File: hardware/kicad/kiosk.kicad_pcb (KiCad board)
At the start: 2 copper layers, 158 x 121 mm, 20 parts, among them J10 TerminalBlock_MaiXu_MX126-5.0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, J11 TerminalBlock_MaiXu_MX126-5.0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, J13 PinHeader_1x09_P2.54mm_Vertic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, J14 PinHeader_1x04_P2.54mm_Vertic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, J3 PinSocket_1x14_P2.54mm_Vertic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, J4 PinSocket_1x06_P2.54mm_Vertic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, J5 PinSocket_1x04_P2.54mm_Vertic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, J6 PinSocket_1x06_P2.54mm_Vertic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, J7 PinSocket_1x07_P2.54mm_Vertic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, J9 PinHeader_1x03_P2.54mm_Vertic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, U1 ESP32-S3-CAM

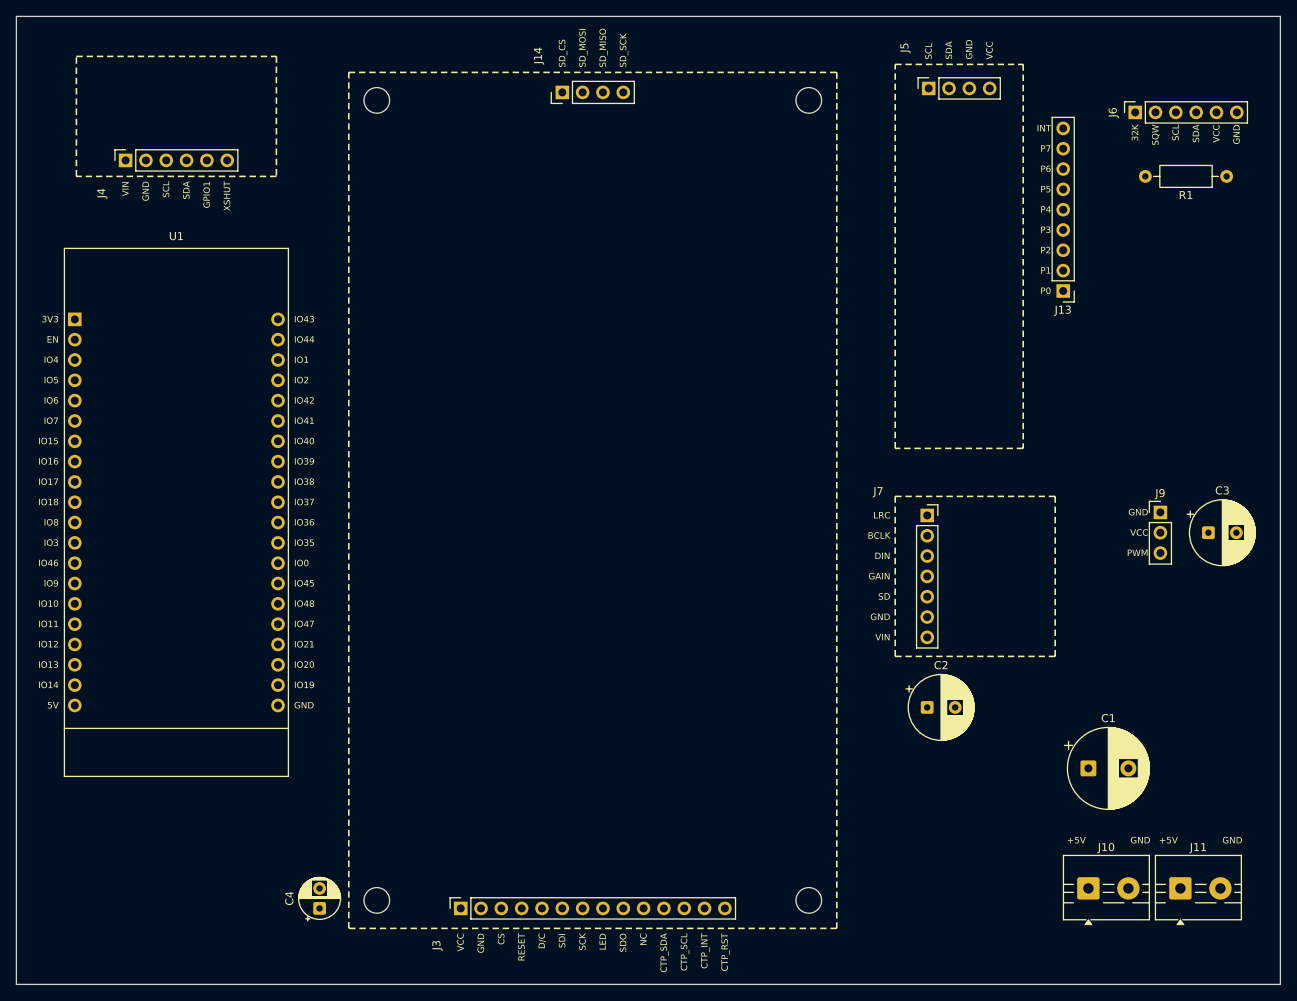
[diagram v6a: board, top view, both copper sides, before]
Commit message: fix(hardware): start every top-row module body on the panel's top edge
The VL53L1X outline began 2 mm above the panel's and the expander's 1 mm
above it. Neither offset was a decision — they are the numbers that were
typed during the rough placement and never revisited — and three
rectangles starting within 2 mm of each other reads as a board nobody
lined up, which is what it was.

All three now start at y 7. The devkit follows the ToF down so the left
column keeps its spacing, and the gap between the ToF's body and the
devkit's courtyard stays 8.75 mm.

Task: E14-T8
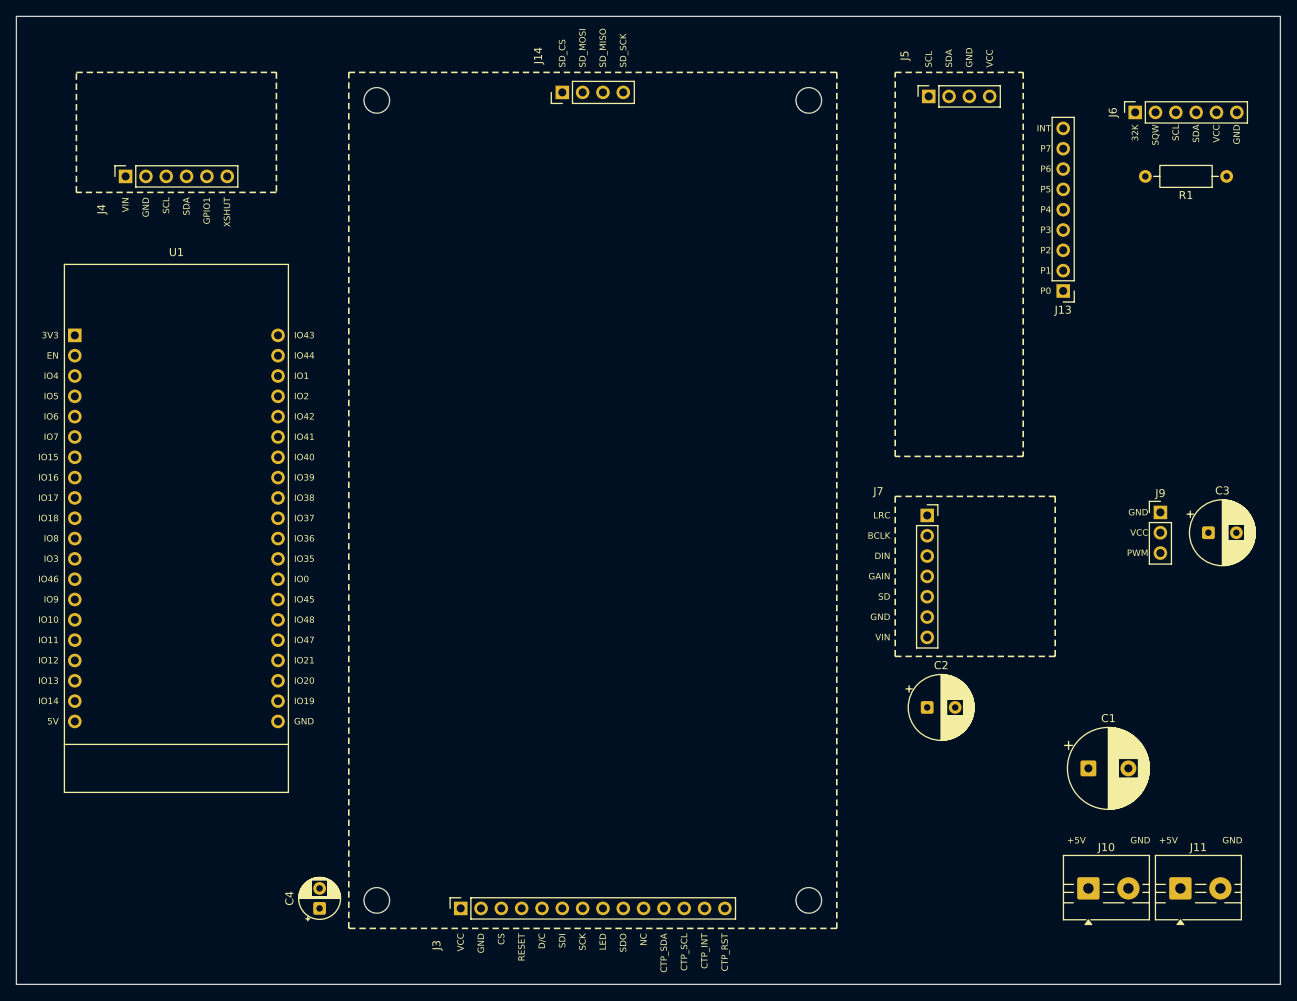
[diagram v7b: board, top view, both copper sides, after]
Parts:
- moved J4 2.00 mm to (13.7, 20.0)
- moved U1 2.00 mm to (20.0, 64.0)
- moved J5 1.00 mm to (114.0, 10.0)
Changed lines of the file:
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@@
 	(footprint "Connector_PinSocket_2.54mm:PinSocket_1x04_P2.54mm_Vertical"
 		(layer "F.Cu")
-		(at 114.04 9 90)
+		(at 114.04 10 90)
 		(descr "Through hole straight socket strip, 1x04, 2.54mm pitch, single row (from Kicad 4.0.7), script generated")
 		(tags "Through hole socket strip THT 1x04 2.54mm single row")
@@
 	(footprint "Connector_PinSocket_2.54mm:PinSocket_1x06_P2.54mm_Vertical"
 		(layer "F.Cu")
-		(at 13.65 18 90)
+		(at 13.65 20 90)
 		(descr "Through hole straight socket strip, 1x06, 2.54mm pitch, single row (from Kicad 4.0.7), script generated")
 		(tags "Through hole socket strip THT 1x06 2.54mm single row")
@@
 	(footprint "kiosk:ESP32-S3-CAM_2x20_P2.54mm_R25.4mm"
 		(layer "F.Cu")
-		(at 20 62)
+		(at 20 64)
 		(descr "GOOUUU ESP32-S3-CAM socket, 2x20 at 2.54 mm, rows 25.4 mm apart - measured on the board and confirmed against a published figure. Pin 1 = 3V3 at top left seen from above with the two USB-C on the bottom edge; the silkscreen bar marks that edge. The outline is deliberately oversized: this board has no datasheet, so its real edge is unmeasured and the courtyard errs wide to keep tall parts out from under it. Keep the USB edge clear for cables, and EN and BOOT reachable on the top face.")
 		(tags "esp32s3 cam devkit socket")
@@
 	)
 	(gr_line
-		(start 7.5 5)
-		(end 32.5 5)
+		(start 7.5 7)
+		(end 32.5 7)
 		(stroke
 			(width 0.2)
@@
 	)
 	(gr_line
-		(start 7.5 20)
-		(end 7.5 5)
+		(start 7.5 22)
+		(end 7.5 7)
 		(stroke
 			(width 0.2)
@@
 	)
 	(gr_line
-		(start 32.5 5)
-		(end 32.5 20)
+		(start 32.5 7)
+		(end 32.5 22)
 		(stroke
 			(width 0.2)
@@
 	)
 	(gr_line
-		(start 32.5 20)
-		(end 7.5 20)
+		(start 32.5 22)
+		(end 7.5 22)
 		(stroke
 			(width 0.2)
@@
 	)
 	(gr_line
-		(start 109.85 6)
-		(end 125.85 6)
+		(start 109.85 7)
+		(end 125.85 7)
 		(stroke
 			(width 0.2)
@@
 	)
 	(gr_line
-		(start 109.85 54)
-		(end 109.85 6)
+		(start 109.85 55)
+		(end 109.85 7)
 		(stroke
 			(width 0.2)
@@
 	)
 	(gr_line
-		(start 125.85 6)
-		(end 125.85 54)
+		(start 125.85 7)
+		(end 125.85 55)
 		(stroke
 			(width 0.2)
@@
 	)
 	(gr_line
-		(start 125.85 54)
-		(end 109.85 54)
+		(start 125.85 55)
+		(end 109.85 55)
 		(stroke
 			(width 0.2)
@@
 	)
 	(gr_text "IO43"
-		(at 34.7 37.87 0)
+		(at 34.7 39.87 0)
 		(layer "F.SilkS")
 		(effects
@@
 	)
 	(gr_text "IO44"
-		(at 34.7 40.41 0)
+		(at 34.7 42.41 0)
 		(layer "F.SilkS")
 		(effects
@@
 	)
 	(gr_text "IO1"
-		(at 34.7 42.95 0)
+		(at 34.7 44.95 0)
 		(layer "F.SilkS")
 		(effects
@@
 	)
 	(gr_text "IO2"
-		(at 34.7 45.49 0)
+		(at 34.7 47.49 0)
 		(layer "F.SilkS")
 		(effects
@@
 	)
 	(gr_text "IO42"
-		(at 34.7 48.03 0)
+		(at 34.7 50.03 0)
 		(layer "F.SilkS")
 		(effects
@@
 	)
 	(gr_text "IO41"
-		(at 34.7 50.57 0)
+		(at 34.7 52.57 0)
 		(layer "F.SilkS")
 		(effects
@@
 	)
 	(gr_text "IO40"
-		(at 34.7 53.11 0)
+		(at 34.7 55.11 0)
 		(layer "F.SilkS")
 		(effects
@@
 	)
 	(gr_text "IO39"
-		(at 34.7 55.65 0)
+		(at 34.7 57.65 0)
 		(layer "F.SilkS")
 		(effects
@@
 	)
 	(gr_text "IO38"
-		(at 34.7 58.19 0)
+		(at 34.7 60.19 0)
 		(layer "F.SilkS")
 		(effects
@@
 	)
 	(gr_text "IO37"
-		(at 34.7 60.73 0)
+		(at 34.7 62.73 0)
 		(layer "F.SilkS")
 		(effects
@@
 	)
 	(gr_text "IO36"
-		(at 34.7 63.27 0)
+		(at 34.7 65.27 0)
 		(layer "F.SilkS")
 		(effects
@@
 	)
 	(gr_text "IO35"
-		(at 34.7 65.81 0)
+		(at 34.7 67.81 0)
 		(layer "F.SilkS")
 		(effects
@@
 	)
 	(gr_text "IO0"
-		(at 34.7 68.35 0)
+		(at 34.7 70.35 0)
 		(layer "F.SilkS")
 		(effects
@@
 	)
 	(gr_text "IO45"
-		(at 34.7 70.89 0)
+		(at 34.7 72.89 0)
 		(layer "F.SilkS")
 		(effects
@@
 	)
 	(gr_text "IO48"
-		(at 34.7 73.43 0)
+		(at 34.7 75.43 0)
 		(layer "F.SilkS")
 		(effects
@@
 	)
 	(gr_text "IO47"
-		(at 34.7 75.97 0)
+		(at 34.7 77.97 0)
 		(layer "F.SilkS")
 		(effects
@@
 	)
 	(gr_text "IO21"
-		(at 34.7 78.51 0)
+		(at 34.7 80.51 0)
 		(layer "F.SilkS")
 		(effects
@@
 	)
 	(gr_text "IO20"
-		(at 34.7 81.05 0)
+		(at 34.7 83.05 0)
 		(layer "F.SilkS")
 		(effects
@@
 	)
 	(gr_text "IO19"
-		(at 34.7 83.59 0)
+		(at 34.7 85.59 0)
 		(layer "F.SilkS")
 		(effects
@@
 	)
 	(gr_text "GND"
-		(at 34.7 86.13 0)
+		(at 34.7 88.13 0)
 		(layer "F.SilkS")
 		(effects
@@
 	)
 	(gr_text "3V3"
-		(at 5.3 37.87 0)
+		(at 5.3 39.87 0)
 		(layer "F.SilkS")
 		(effects
@@
 	)
 	(gr_text "EN"
-		(at 5.3 40.41 0)
+		(at 5.3 42.41 0)
 		(layer "F.SilkS")
 		(effects
@@
 	)
 	(gr_text "IO4"
-		(at 5.3 42.95 0)
+		(at 5.3 44.95 0)
 		(layer "F.SilkS")
 		(effects
@@
 	)
 	(gr_text "IO5"
-		(at 5.3 45.49 0)
+		(at 5.3 47.49 0)
 		(layer "F.SilkS")
 		(effects
@@
 	)
 	(gr_text "IO6"
-		(at 5.3 48.03 0)
+		(at 5.3 50.03 0)
 		(layer "F.SilkS")
 		(effects
@@
 	)
 	(gr_text "IO7"
-		(at 5.3 50.57 0)
+		(at 5.3 52.57 0)
 		(layer "F.SilkS")
 		(effects
@@
 	)
 	(gr_text "IO15"
-		(at 5.3 53.11 0)
+		(at 5.3 55.11 0)
 		(layer "F.SilkS")
 		(effects
@@
 	)
 	(gr_text "IO16"
-		(at 5.3 55.65 0)
+		(at 5.3 57.65 0)
 		(layer "F.SilkS")
 		(effects
@@
 	)
 	(gr_text "IO17"
-		(at 5.3 58.19 0)
+		(at 5.3 60.19 0)
 		(layer "F.SilkS")
 		(effects
@@
 	)
 	(gr_text "IO18"
-		(at 5.3 60.73 0)
+		(at 5.3 62.73 0)
 		(layer "F.SilkS")
 		(effects
@@
 	)
 	(gr_text "IO8"
-		(at 5.3 63.27 0)
+		(at 5.3 65.27 0)
 		(layer "F.SilkS")
 		(effects
@@
 	)
 	(gr_text "IO3"
-		(at 5.3 65.81 0)
+		(at 5.3 67.81 0)
 		(layer "F.SilkS")
 		(effects
@@
 	)
 	(gr_text "IO46"
-		(at 5.3 68.35 0)
+		(at 5.3 70.35 0)
 		(layer "F.SilkS")
 		(effects
@@
 	)
 	(gr_text "IO9"
-		(at 5.3 70.89 0)
+		(at 5.3 72.89 0)
 		(layer "F.SilkS")
 		(effects
@@
 	)
 	(gr_text "IO10"
-		(at 5.3 73.43 0)
+		(at 5.3 75.43 0)
 		(layer "F.SilkS")
 		(effects
@@
 	)
 	(gr_text "IO11"
-		(at 5.3 75.97 0)
+		(at 5.3 77.97 0)
 		(layer "F.SilkS")
 		(effects
@@
 	)
 	(gr_text "IO12"
-		(at 5.3 78.51 0)
+		(at 5.3 80.51 0)
 		(layer "F.SilkS")
 		(effects
@@
 	)
 	(gr_text "IO13"
-		(at 5.3 81.05 0)
+		(at 5.3 83.05 0)
 		(layer "F.SilkS")
 		(effects
@@
 	)
 	(gr_text "IO14"
-		(at 5.3 83.59 0)
+		(at 5.3 85.59 0)
 		(layer "F.SilkS")
 		(effects
@@
 	)
 	(gr_text "5V"
-		(at 5.3 86.13 0)
+		(at 5.3 88.13 0)
 		(layer "F.SilkS")
 		(effects
@@
 	)
 	(gr_text "SCL"
-		(at 114.04 5.4 90)
+		(at 114.04 6.4 90)
 		(layer "F.SilkS")
 		(effects
@@
 	)
 	(gr_text "SDA"
-		(at 116.58 5.4 90)
+		(at 116.58 6.4 90)
 		(layer "F.SilkS")
 		(effects
@@
 	)
 	(gr_text "GND"
-		(at 119.12 5.4 90)
+		(at 119.12 6.4 90)
 		(layer "F.SilkS")
 		(effects
@@
 	)
 	(gr_text "VCC"
-		(at 121.66 5.4 90)
+		(at 121.66 6.4 90)
 		(layer "F.SilkS")
 		(effects
@@
 	)
 	(gr_text "VIN"
-		(at 13.65 20.6 90)
+		(at 13.65 22.6 90)
 		(layer "F.SilkS")
 		(effects
@@
 	)
 	(gr_text "GND"
-		(at 16.19 20.6 90)
+		(at 16.19 22.6 90)
 		(layer "F.SilkS")
 		(effects
@@
 	)
 	(gr_text "SCL"
-		(at 18.73 20.6 90)
+		(at 18.73 22.6 90)
 		(layer "F.SilkS")
 		(effects
@@
 	)
 	(gr_text "SDA"
-		(at 21.27 20.6 90)
+		(at 21.27 22.6 90)
 		(layer "F.SilkS")
 		(effects
@@
 	)
 	(gr_text "GPIO1"
-		(at 23.81 20.6 90)
+		(at 23.81 22.6 90)
 		(layer "F.SilkS")
 		(effects
@@
 	)
 	(gr_text "XSHUT"
-		(at 26.35 20.6 90)
+		(at 26.35 22.6 90)
 		(layer "F.SilkS")
 		(effects

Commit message: feat(hardware): give the carrier its own five mounting holes
H1 to H4 bolt the panel to this board. Nothing bolted this board to
anything — the whole assembly would have hung in the case on the panel's
own standoffs, with the two screw terminals, which are the one place a
person applies force to the board, at the unsupported end.

Five M3 holes, same size as the panel's so the build needs one screw.
Two of them do not get their corner: the ToF module stands in the top left
and the terminals in the bottom right, so those slide along an edge to the
nearest place a 6.9 mm courtyard actually fits.

Those places were found by sweeping the board for free space rather than
guessed — a first pass put one at (130, 116) from reading a region's
bounding box, and check_pcb caught it overlapping J10.

Task: E14-T8
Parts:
- added H5: MountingHole_3.2mm_M3, MountingHole:MountingHole_3.2mm_M3, F.Cu at (4.00, 26.0)
- added H6: MountingHole_3.2mm_M3, MountingHole:MountingHole_3.2mm_M3, F.Cu at (154.0, 4.00)
- added H7: MountingHole_3.2mm_M3, MountingHole:MountingHole_3.2mm_M3, F.Cu at (154.0, 98.5)
- added H8: MountingHole_3.2mm_M3, MountingHole:MountingHole_3.2mm_M3, F.Cu at (118.0, 117.0)
- added H9: MountingHole_3.2mm_M3, MountingHole:MountingHole_3.2mm_M3, F.Cu at (4.00, 117.0)
